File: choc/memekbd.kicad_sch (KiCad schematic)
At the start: 192 parts, among them J1 USB_B_Micro, J2 USB_B_Micro, SW1 SW_Push, SW10 SW_Push, SW11 SW_Push, SW12 SW_Push, SW13 SW_Push, SW14 SW_Push, SW15 SW_Push, SW16 SW_Push, SW17 SW_Push, SW18 SW_Push, SW19 SW_Push, SW2 SW_Push, SW20 SW_Push, SW21 SW_Push, SW22 SW_Push, SW23 SW_Push, SW24 SW_Push, SW25 SW_Push, SW26 SW_Push, SW27 SW_Push, SW28 SW_Push, SW29 SW_Push, SW3 SW_Push, SW30 SW_Push, SW31 SW_Push, SW32 SW_Push, SW33 SW_Push, SW34 SW_Push, SW35 SW_Push, SW36 SW_Push, SW37 SW_Push, SW38 SW_Push, SW39 SW_Push, SW4 SW_Push, SW40 SW_Push, SW41 SW_Push, SW42 SW_Push, SW43 SW_Push, SW44 SW_Push, SW45 SW_Push, SW46 SW_Push, SW47 SW_Push, SW48 SW_Push, SW49 SW_Push, SW5 SW_Push, SW50 SW_Push, SW6 SW_Push, SW7 SW_Push, SW8 SW_Push, SW9 SW_Push, U1 ProMicro, U2 ProMicro

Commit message: fix diodes not having vertical space in choc
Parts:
- removed C11, C12, C13, C14, C16, C17, C18, C19, C20, C21, C22, C23, C6, C7, C8, C9: 0.1uF, Capacitor_THT:C_Disc_D6.0mm_W2.5mm_P5.00mm, symbol Device:C_Small
- removed H16, H3: MountingHole_Pad, MountingHole:MountingHole_3.2mm_M3_ISO7380_Pad, symbol Mechanical:MountingHole_Pad
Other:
- moved on the sheet: C1, C2, C3, C4

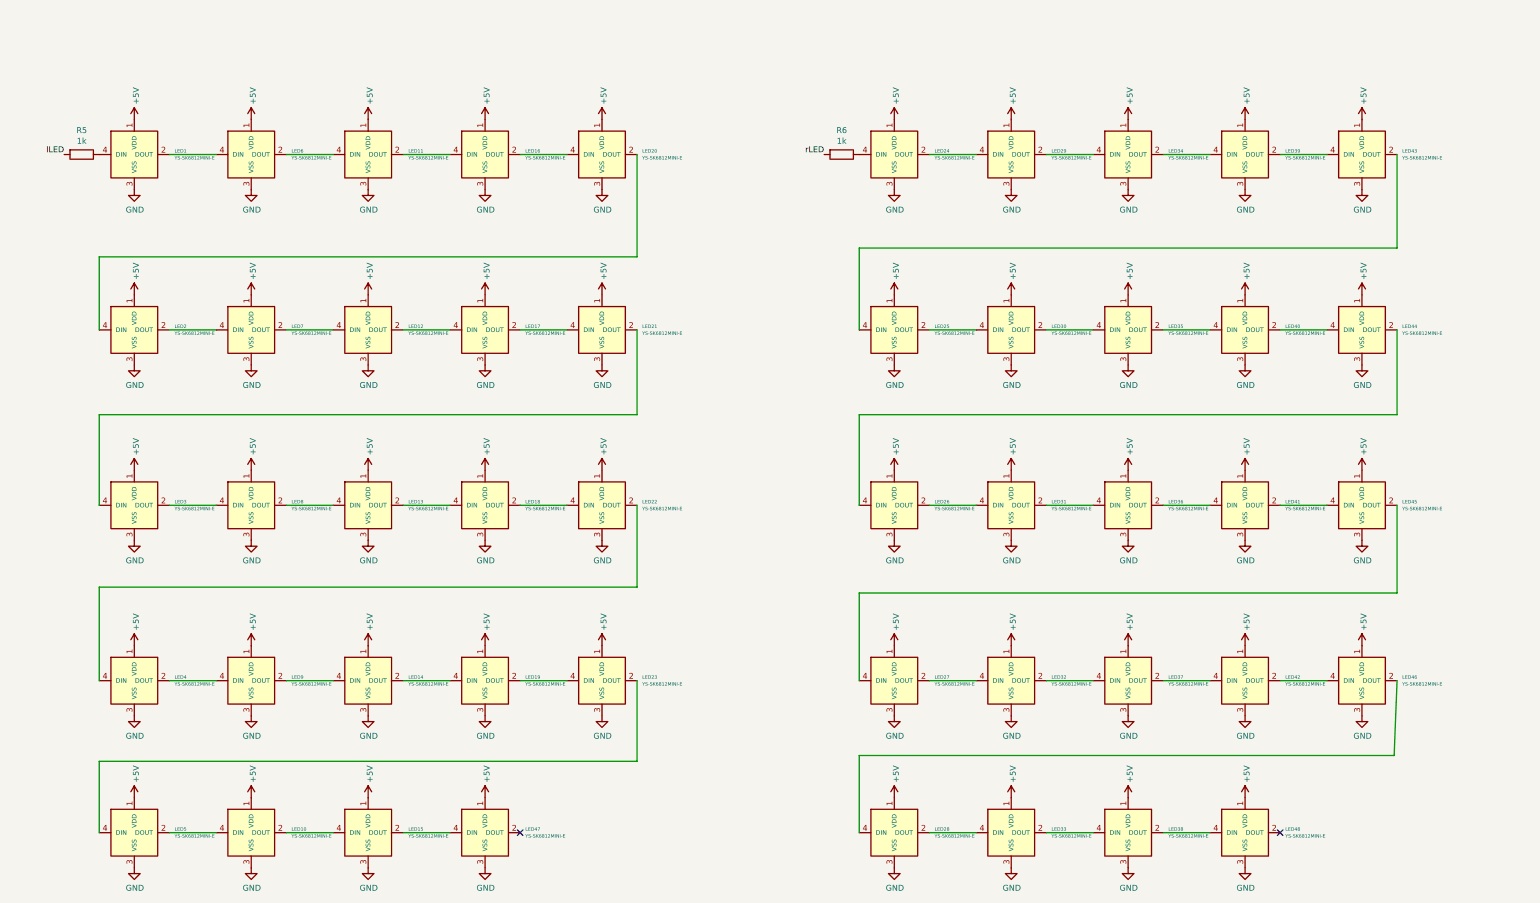
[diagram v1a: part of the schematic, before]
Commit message: remove leds from choc
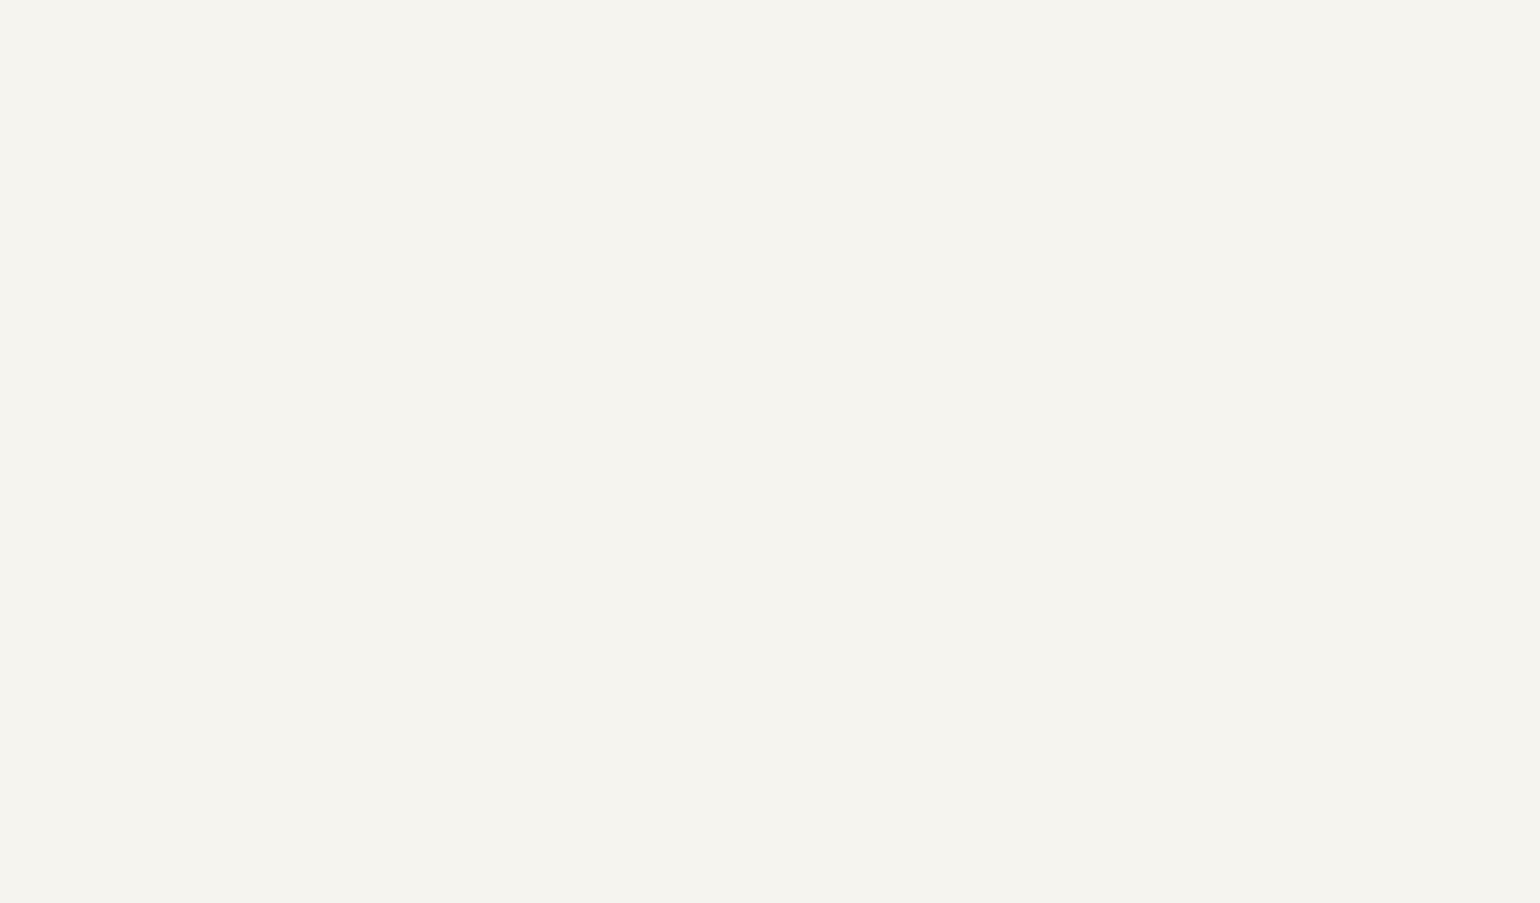
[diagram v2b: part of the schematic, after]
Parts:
- removed LED1, LED10, LED11, LED12, LED13, LED14, LED15, LED16, LED17, LED18, LED19, LED2, LED20, LED21, LED22, LED23, LED24, LED25, LED26, LED27, LED28, LED29, LED3, LED30, LED31, LED32, LED33, LED34, LED35, LED36, LED37, LED38, LED39, LED4, LED40, LED41, LED42, LED43, LED44, LED45, LED46, LED47, LED48, LED5, LED6, LED7, LED8, LED9: YS-SK6812MINI-E, kbd:YS-SK6812MINI-E, symbol kbd:YS-SK6812MINI-E
- removed R5, R6: 1k, Resistor_THT:R_Axial_DIN0207_L6.3mm_D2.5mm_P7.62mm_Horizontal, symbol Device:R
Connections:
- no-connect marks 16 -> 14

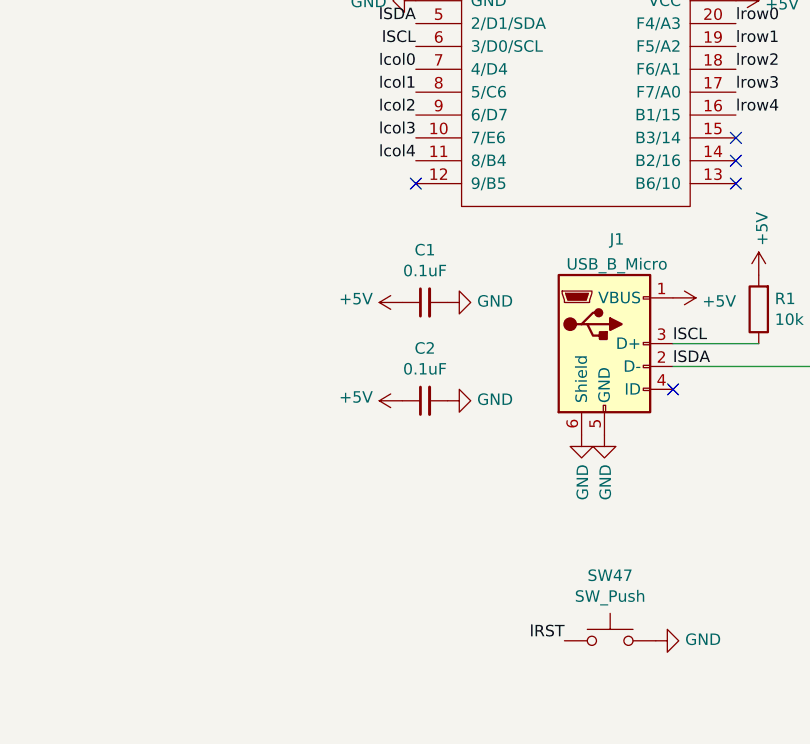
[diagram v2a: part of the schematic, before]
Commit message: add buzzer to schematic
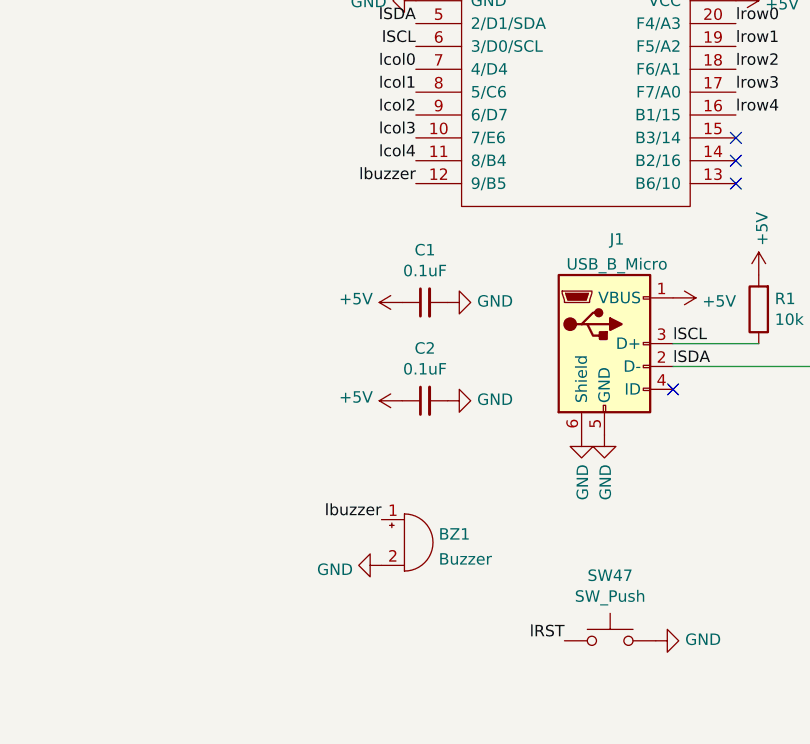
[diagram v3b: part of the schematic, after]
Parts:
- added BZ1: Buzzer, Buzzer_Beeper:MagneticBuzzer_PUI_AT-0927-TT-6-R, symbol Device:Buzzer
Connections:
- net GND: now also BZ1.2 (+)
- net lbuzzer: now reaches U1.12 (9/B5)
- net lbuzzer: now also BZ1.1 (-)
- no-connect marks 14 -> 13
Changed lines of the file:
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@@
   (junction (at 306.07 88.9) (diameter 1.016) (color 0 0 0 0))
   (no_connect (at 375.92 49.53))
-  (no_connect (at 375.92 74.93))
   (no_connect (at 404.495 97.79))
   (no_connect (at 411.48 46.99))
@@
     (effects (font (size 1.27 1.27)) (justify left bottom))
   )
+  (label "lbuzzer" (at 372.11 112.268 180)
+    (effects (font (size 1.27 1.27)) (justify right bottom))
+  )
   (label "lLED" (at 375.92 46.99 180)
     (effects (font (size 1.27 1.27)) (justify right bottom))
@@
     (effects (font (size 1.27 1.27)) (justify right bottom))
   )
+  (label "lbuzzer" (at 375.92 74.93 180)
+    (effects (font (size 1.27 1.27)) (justify right bottom))
+  )
   (label "lRST" (at 392.43 125.73 180)
     (effects (font (size 1.27 1.27)) (justify right bottom))
@@
     (pin "1")
   )
+  (symbol (lib_id "power:GND") (at 372.11 117.348 270) (unit 1)
+    (in_bom yes) (on_board yes) (fields_autoplaced)
+    (property "Reference" "#PWR0101" (id 0) (at 365.76 117.348 0)
+      (effects (font (size 1.27 1.27)) hide)
+    )
+    (property "Value" "GND" (id 1) (at 368.935 117.827 90)
+      (effects (font (size 1.27 1.27)) (justify right))
+    )
+    (property "Footprint" "" (id 2) (at 372.11 117.348 0)
+      (effects (font (size 1.27 1.27)) hide)
+    )
+    (property "Datasheet" "" (id 3) (at 372.11 117.348 0)
+      (effects (font (size 1.27 1.27)) hide)
+    )
+    (pin "1")
+  )
   (symbol (lib_id "power:GND") (at 375.92 52.07 270) (unit 1)
     (in_bom yes) (on_board yes)
@@
     (pin "2")
   )
+  (symbol (lib_id "Device:Buzzer") (at 374.65 114.808 0) (unit 1)
+    (in_bom yes) (on_board yes) (fields_autoplaced)
+    (property "Reference" "BZ1" (id 0) (at 378.4601 113.8995 0)
+      (effects (font (size 1.27 1.27)) (justify left))
+    )
+    (property "Value" "Buzzer" (id 1) (at 378.4601 116.6746 0)
+      (effects (font (size 1.27 1.27)) (justify left))
+    )
+    (property "Footprint" "Buzzer_Beeper:MagneticBuzzer_PUI_AT-0927-TT-6-R" (id 2) (at 374.015 112.268 90)
+      (effects (font (size 1.27 1.27)) hide)
+    )
+    (property "Datasheet" "~" (id 3) (at 374.015 112.268 90)
+      (effects (font (size 1.27 1.27)) hide)
+    )
+    (pin "1")
+    (pin "2")
+  )
   (symbol (lib_id "Connector:USB_B_Micro") (at 396.875 92.71 0) (unit 1)
     (in_bom yes) (on_board yes) (fields_autoplaced)
@@
       (reference "#PWR012") (unit 1) (value "GND") (footprint "")
     )
+    (path "/e72d9d26-68d2-485e-ac98-97dba7b07fe6"
+      (reference "#PWR0101") (unit 1) (value "GND") (footprint "")
+    )
     (path "/00000000-0000-0000-0000-000060d9be71"
       (reference "#PWR0122") (unit 1) (value "GND") (footprint "")
@@
       (reference "#PWR0175") (unit 1) (value "GND") (footprint "")
     )
+    (path "/723b5371-e4f6-4249-95e2-50d45d156d39"
+      (reference "BZ1") (unit 1) (value "Buzzer") (footprint "Buzzer_Beeper:MagneticBuzzer_PUI_AT-0927-TT-6-R")
+    )
     (path "/00000000-0000-0000-0000-0000610a94ce"

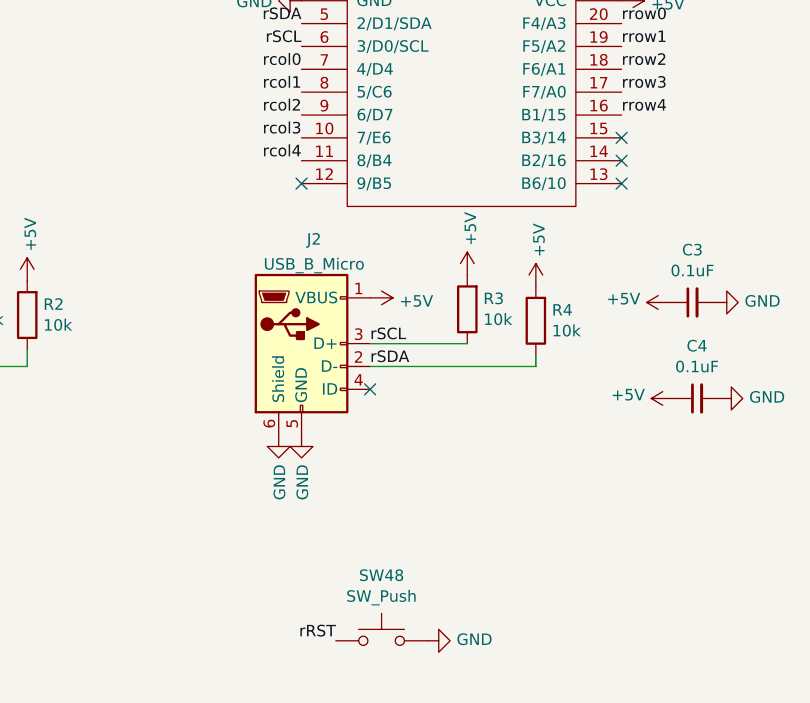
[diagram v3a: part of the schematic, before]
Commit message: add buzzer to pcb
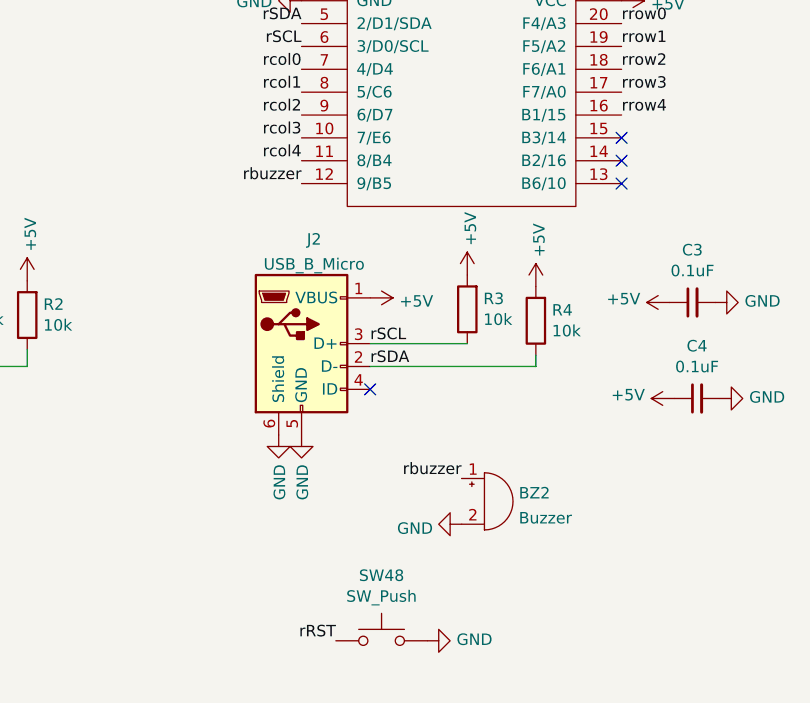
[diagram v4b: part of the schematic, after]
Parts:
- added BZ2: Buzzer, Buzzer_Beeper:MagneticBuzzer_PUI_AT-0927-TT-6-R, symbol Device:Buzzer
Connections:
- net GND: now also BZ2.2 (+)
- net rbuzzer: now reaches U2.12 (9/B5)
- net rbuzzer: now also BZ2.1 (-)
- no-connect marks 13 -> 12
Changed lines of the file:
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@@
   (no_connect (at 411.48 74.93))
   (no_connect (at 452.12 49.53))
-  (no_connect (at 452.12 74.93))
   (no_connect (at 459.74 97.79))
   (no_connect (at 487.68 46.99))
@@
     (effects (font (size 1.27 1.27)) (justify right bottom))
   )
+  (label "rbuzzer" (at 452.12 74.93 180)
+    (effects (font (size 1.27 1.27)) (justify right bottom))
+  )
   (label "rRST" (at 455.93 125.73 180)
     (effects (font (size 1.27 1.27)) (justify right bottom))
@@
     (effects (font (size 1.27 1.27)) (justify left bottom))
   )
+  (label "rbuzzer" (at 469.9 107.696 180)
+    (effects (font (size 1.27 1.27)) (justify right bottom))
+  )
   (label "rRST" (at 487.68 52.07 0)
     (effects (font (size 1.27 1.27)) (justify left bottom))
@@
     (pin "1")
   )
+  (symbol (lib_id "power:GND") (at 469.9 112.776 270) (unit 1)
+    (in_bom yes) (on_board yes) (fields_autoplaced)
+    (property "Reference" "#PWR0102" (id 0) (at 463.55 112.776 0)
+      (effects (font (size 1.27 1.27)) hide)
+    )
+    (property "Value" "GND" (id 1) (at 466.725 113.255 90)
+      (effects (font (size 1.27 1.27)) (justify right))
+    )
+    (property "Footprint" "" (id 2) (at 469.9 112.776 0)
+      (effects (font (size 1.27 1.27)) hide)
+    )
+    (property "Datasheet" "" (id 3) (at 469.9 112.776 0)
+      (effects (font (size 1.27 1.27)) hide)
+    )
+    (pin "1")
+  )
   (symbol (lib_id "power:GND") (at 487.68 49.53 90) (unit 1)
     (in_bom yes) (on_board yes)
@@
     (pin "2")
   )
+  (symbol (lib_id "Device:Buzzer") (at 472.44 110.236 0) (unit 1)
+    (in_bom yes) (on_board yes) (fields_autoplaced)
+    (property "Reference" "BZ2" (id 0) (at 476.2501 109.3275 0)
+      (effects (font (size 1.27 1.27)) (justify left))
+    )
+    (property "Value" "Buzzer" (id 1) (at 476.2501 112.1026 0)
+      (effects (font (size 1.27 1.27)) (justify left))
+    )
+    (property "Footprint" "Buzzer_Beeper:MagneticBuzzer_PUI_AT-0927-TT-6-R" (id 2) (at 471.805 107.696 90)
+      (effects (font (size 1.27 1.27)) hide)
+    )
+    (property "Datasheet" "~" (id 3) (at 471.805 107.696 90)
+      (effects (font (size 1.27 1.27)) hide)
+    )
+    (pin "1")
+    (pin "2")
+  )
   (symbol (lib_id "Connector:USB_B_Micro") (at 396.875 92.71 0) (unit 1)
     (in_bom yes) (on_board yes) (fields_autoplaced)
@@
       (reference "#PWR0101") (unit 1) (value "GND") (footprint "")
     )
+    (path "/e997906a-9e9f-4031-8024-96eea2e83694"
+      (reference "#PWR0102") (unit 1) (value "GND") (footprint "")
+    )
     (path "/00000000-0000-0000-0000-000060d9be71"
       (reference "#PWR0122") (unit 1) (value "GND") (footprint "")
@@
       (reference "BZ1") (unit 1) (value "Buzzer") (footprint "Buzzer_Beeper:MagneticBuzzer_PUI_AT-0927-TT-6-R")
     )
+    (path "/8c027bcd-46aa-4a2a-8e4c-340404a780b5"
+      (reference "BZ2") (unit 1) (value "Buzzer") (footprint "Buzzer_Beeper:MagneticBuzzer_PUI_AT-0927-TT-6-R")
+    )
     (path "/00000000-0000-0000-0000-0000610a94ce"
